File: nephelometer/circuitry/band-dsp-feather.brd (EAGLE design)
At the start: 95 x 55 mm, 67 parts, among them IC1 LM4041CILP, IC2 AD822N, IC3 MCP6S21, IC4 LP2950ACZ-3.3, J1 RJ11-6PTH, Q1 IRLB8721, T1 2N2222, T2 2N2222, T3 2N2222, T4 2N2222, T5 2N2222, T6 2N2222

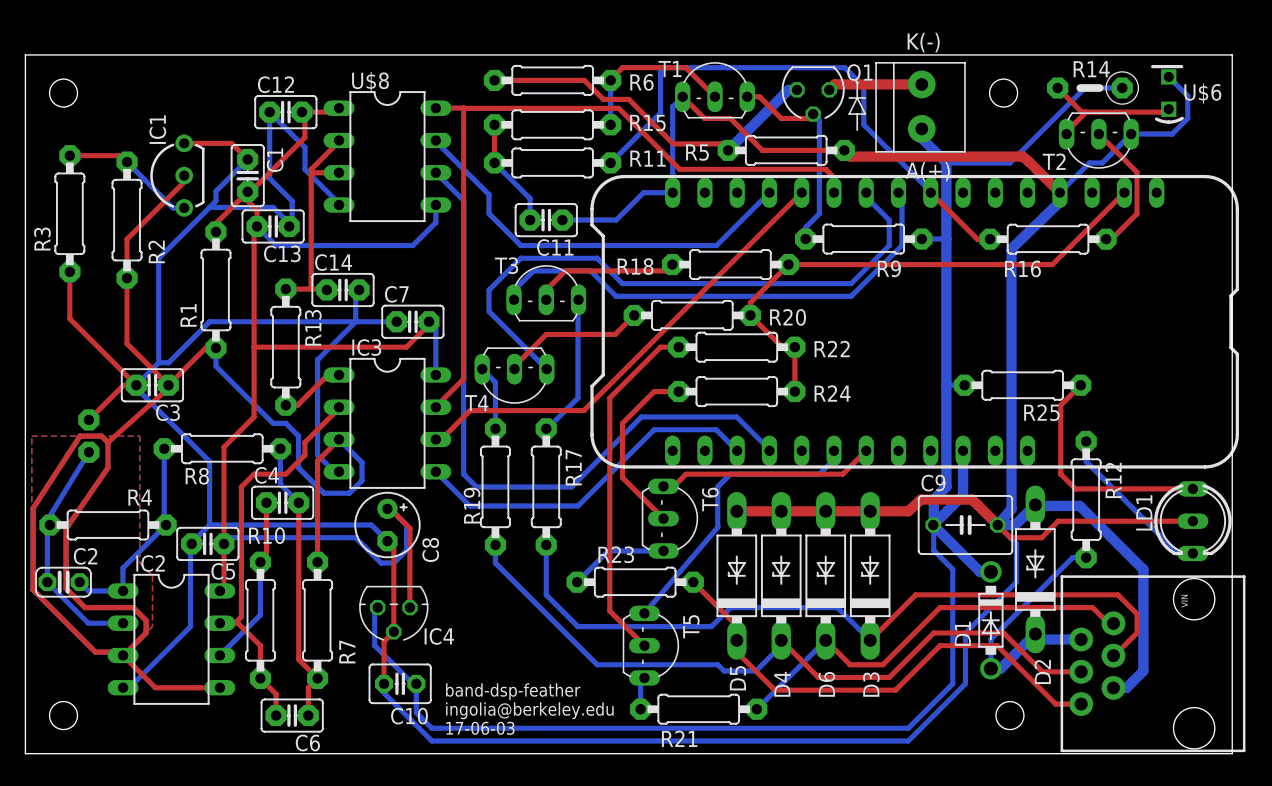
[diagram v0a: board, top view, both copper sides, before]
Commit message: Feather motor controller board with ESD protection and up to 4 motors or 2 motors plus stepper
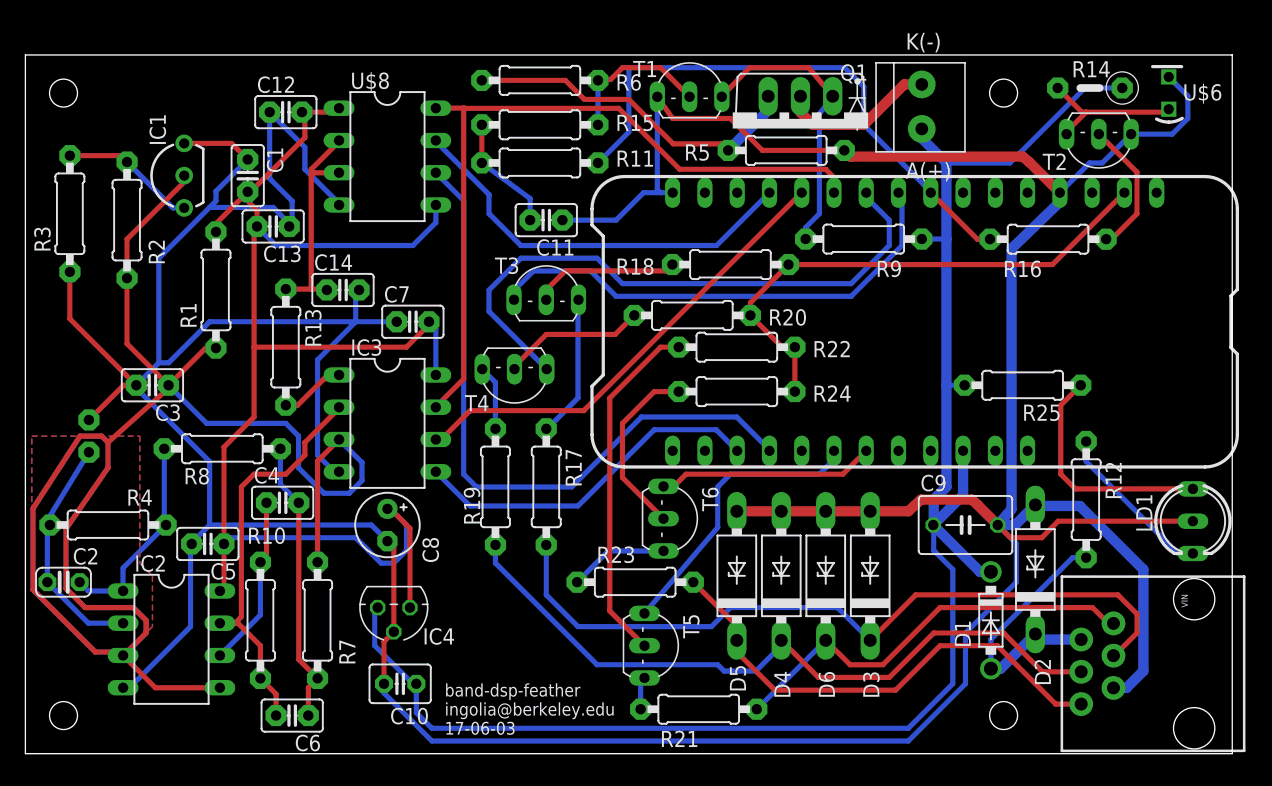
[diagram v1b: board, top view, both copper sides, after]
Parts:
- D2: value (none) -> 5V
- D3, D4, D5, D6: value (none) -> 12V
- Q1: device transistor-small-signal:SOT54E -> ingolia:TO220BV
- R17, R19, R21, R23: value 1K0 -> 1K5
- moved T1 2.00 mm to (52.3, 58.0)
- moved Q1 1.12 mm to (61.0, 56.8)
- moved R11 1.00 mm to (40.5, 54.5)
- moved R15 1.00 mm to (40.5, 51.5)
- moved R6 1.00 mm to (40.5, 58.0)
- moved U$3 0.50 mm to (77.0, 8.00)
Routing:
- net N$8: track 16.5 -> 22.9 mm
- net N$18: track 7.46 -> 12.5 mm
- net LED_CTRL: track 42.4 -> 44.3 mm
- net 1V65: track 169.3 -> 171.0 mm
- net GND: track 384.9 -> 386.5 mm
- net N$13: track 13.1 -> 12.0 mm
- net N$14: track 28.1 -> 27.2 mm
- net N$15: track 8.66 -> 9.42 mm

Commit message: Finalized Feather nephelometer with separate ADC and 4 robust motor controls
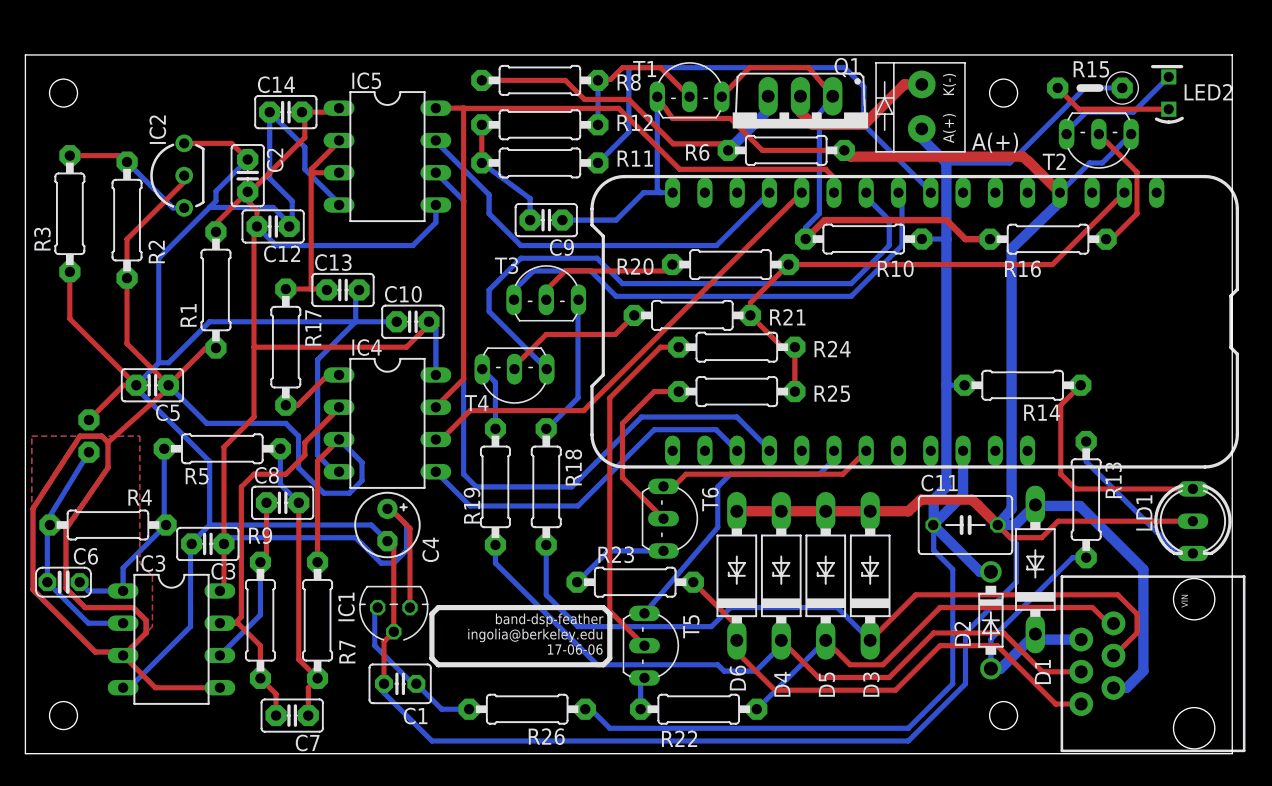
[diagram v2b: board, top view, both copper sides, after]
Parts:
- added R26: 8.2R, adafruit:0207/9
- C1: value 100nF -> 1µF; device adafruit:C025-025X050 -> adafruit:C025-030X050
- C10: value 1µF -> 100nF; device adafruit:C025-030X050 -> adafruit:C025-025X050
- C11: value 1.2nF -> 22µF; device adafruit:C025-025X050 -> adafruit:C050-045X075
- C12: value 100nF -> 1uF
- C13: value 1uF -> 1.2nF
- C14: value 1.2nF -> 100nF
- C2: value 3pF -> 100nF; device adafruit:C025-024X044 -> adafruit:C025-025X050
- C3: value 100n -> 100nF
- C4: value 1.2nF -> 10µF; device adafruit:C025-025X050 -> adafruit:E2,5-5
- C5: value 100nF -> 100n
- C6: value 1.2nF -> 3pF; device adafruit:C025-025X050 -> adafruit:C025-024X044
- C7: value 100nF -> 1.2nF
- C8: value 10µF -> 1.2nF; device adafruit:E2,5-5 -> adafruit:C025-025X050
- C9: value 22µF -> 1.2nF; device adafruit:C050-045X075 -> adafruit:C025-025X050
- D1: value 1N5817-T -> 5V; device diode:DO41-7.6 -> diode:F126Z10
- D2: value 5V -> 1N5817-T; device diode:F126Z10 -> diode:DO41-7.6
- IC1: value LM4041CILP -> LP2950ACZ-3.3; device texas:LP_O-PBCY-W3 -> v-reg:TO92
- IC2: value AD822N -> LM4041CILP; device analog-devices:DIL08 -> texas:LP_O-PBCY-W3
- IC3: value MCP6S21 -> AD822N; device ingolia:DIL08 -> analog-devices:DIL08
- IC4: value LP2950ACZ-3.3 -> MCP6S21; device v-reg:TO92 -> ingolia:DIL08
- R10: value 133K -> 10K
- R12: value 470R -> 1k5
- R13: value 330R -> 470R
- R14: device adafruit:0207/5V -> adafruit:0207/9
- R15: value 1k5 -> 470R; device adafruit:0207/9 -> adafruit:0207/5V
- R16: value 1k5 -> 33k
- R17: value 1K5 -> 330R
- R18, R22: value 33K -> 1K5
- R21: value 1K5 -> 33K
- R25: value 470R -> 33K
- R5: value 8R2 -> 6K65
- R6: value 3K3 -> 8R2
- R8: value 6K65 -> 3K3
- R9: value 10K -> 133K
- moved R13 64.1 mm to (83.5, 25.0)
- moved R10 56.2 mm to (66.0, 45.5), turned to 0 degrees
- moved R9 56.2 mm to (18.5, 15.5), turned to 270 degrees
- moved R12 50.5 mm to (40.5, 51.5), turned to 0 degrees
- moved R5 50.2 mm to (15.5, 29.0)
- moved R15 43.7 mm to (83.8, 57.4), turned to 180 degrees
- moved C1 41.8 mm to (29.5, 10.5), turned to 180 degrees
- moved C11 40.8 mm to (74.0, 23.0), turned to 0 degrees
- moved C9 40.8 mm to (41.0, 47.0), turned to 180 degrees
- moved R8 38.3 mm to (40.5, 58.0)
- moved IC1 37.8 mm to (29.0, 16.5), turned to 180 degrees
- moved IC2 36.5 mm to (12.5, 50.5), turned to 90 degrees
- moved C2 35.1 mm to (17.5, 50.5), turned to 270 degrees
- moved C7 32.4 mm to (21.0, 8.00), turned to 180 degrees
- moved R21 31.0 mm to (52.5, 39.5), turned to 180 degrees
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- renumbered U$6 to LED2, U$7 to IC6, U$8 to IC5
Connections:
- new net N$12: LED2.K, T2.C
- new net N$24: C1.1, IC1.3, R26.2
- net +3V3: now also C10.2, C14.2, C2.2, C3.1, C4.+, IC1.1, IC4.8; no longer C1.2, C13.2, C5.1, C7.2, C8.+, IC2.8, IC4.1
- net +5V: now also C11.1, D2.C, R10.2, R14.2, R15.1, R26.1; no longer C10.1, C9.1, D1.C, IC4.3, R14.1, R25.2, R9.2
- net 1V65: now also C5.1, IC2.2, IC3.5, IC4.3; no longer C3.1, IC1.2, IC2.3, IC2.5
- net BPF: now also C7.2, IC3.7, IC4.2, R9.2; no longer C6.2, IC2.7, IC3.2, R10.2
- net CS_PGA: now also IC4.5; no longer IC3.5
- net FB: now also C6.1, IC3.2; no longer C2.1, IC2.2
- net GND: now also C1.2, C10.1, C11.2, C13.2, C14.1, C2.1, C4.-, C9.1, D1.A, IC1.2, IC2.3, IC4.4, R6.1; no longer C1.1, C10.2, C11.1, C13.1, C14.2, C7.1, C8.-, C9.2, D2.A, IC1.3, IC2.4, IC4.2, LED2.K, R5.1
- net LED_CTRL: now also R12.2; no longer R15.2, R16.1
- net MOSI: now also IC4.6; no longer IC3.6
- net MOT1: now also R18.2; no longer R17.2
- net MOT3: now also D5.C, R22.2; no longer D6.C, R21.2
- net MOT4: now also D6.C; no longer D5.C
- net N$11: now also R15.2; no longer R14.2, T2.C
- net N$13: now also R8.1; no longer R6.1
- net N$14: now also R8.2; no longer R5.2
- net N$15: now also C9.2, R12.1; no longer C11.2, R15.1
- net N$19: now also R18.1; no longer R17.1
- net N$2: now also R21.2; no longer R20.2
- net N$20: now also R20.2; no longer R18.2
- net N$21: now also R25.2; no longer R24.2
- net N$22: now also R13.1; no longer R12.1
- net N$23: now also C13.1, R17.1; no longer C14.1, R13.1
- net N$3: now also C7.1, C8.2, R5.1; no longer C4.2, C6.1, R8.1
- net N$35: now also IC2.1; no longer IC1.1
- net N$4: now also IC4.1, R17.2; no longer IC3.1, R13.2
- net N$5: now also R22.1; no longer R21.1
- net N$6: now also R24.2; no longer R22.2
- net N$7: now also R14.1; no longer R25.1
- net N$8: now also R10.1, R16.1; no longer R9.1
- net N$9: now also C8.1, IC3.6, R9.1; no longer C4.1, IC2.6, R10.1
- net SCK: now also IC4.7; no longer IC3.7
- net TIA: now also C6.2, IC3.1, R5.2; no longer C2.2, IC2.1, R8.2
- net VDD: now also R21.1, R25.1; no longer R18.1, R22.1
- net VEXT: now also D1.C, D2.A, R13.2; no longer D1.A, D2.C, R12.2
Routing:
- net +5V: track 132.2 -> 109.1 mm
- net N$8: track 22.9 -> 38.6 mm
- net N$24: track 0.00 -> 12.6 mm
- net N$12: track 0.00 -> 10.0 mm
- net GND: track 386.5 -> 377.6 mm
- net LED_CTRL: track 44.3 -> 38.1 mm
- net N$11: track 12.0 -> 9.43 mm
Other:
- board text added: "A(+)"
- board text added: "band-dsp-feather ingolia@berkeley.edu 17-06-06"
- board text removed: "band-dsp-feather ingolia@berkeley.edu 17-06-03"

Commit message: Minor updates after test assembly
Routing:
- net 1V65: track 171.0 -> 172.5 mm
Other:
- board text added: "band-dsp-feather ingolia@berkeley.edu 17-06-22"
- board text removed: "band-dsp-feather ingolia@berkeley.edu 17-06-06"
